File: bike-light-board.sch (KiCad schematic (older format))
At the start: 104 parts, among them J1 KH-TYPE-C-16P, J2 S2B-PH-SM4-TB, P2 WirePad, P3 WirePad, Q1 HX2301A, Q2 L2N7002DW1T1G, Q3 HX2301A, Q4 SMD0805-20, Q5 HX2301A, SW1 SW_Push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

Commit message: update flash chip to 4MB and divider for VBUS
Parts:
- R28: value 47k -> 10k; JCLPCB Part Number C25792 -> C25744; LCSC Part Number C380741 -> (none)
- R29: value 47k -> 5k1; JCLPCB Part Number C25792 -> C25905; LCSC Part Number C380741 -> (none)
- U4: value P25Q40H-SSH-IT -> P25Q32H-SSH-IT; symbol cb_ICs_Memory:P25Q40H-SSH-IT -> cb_ICs_Memory:P25Q32H-SSH-IT; JCLPCB Part Number C194873 -> C194874; Size (none) -> 4MB
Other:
- note removed: "4M external flash"
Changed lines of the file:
@@
 $EndComp
 $Comp
-L cb_ICs_Memory:P25Q40H-SSH-IT U4
+L cb_ICs_Memory:P25Q32H-SSH-IT U4
 U 1 1 610A95B7
 P 7150 8300
 F 0 "U4" H 7630 8296 50  0000 L CNN
-F 1 "P25Q40H-SSH-IT" H 7630 8205 50  0000 L CNN
+F 1 "P25Q32H-SSH-IT" H 7630 8205 50  0000 L CNN
 F 2 "Package_SO:SOIC-8_3.9x4.9mm_P1.27mm" H 7150 7700 50  0001 C CNN
 F 3 "https://www.adestotech.com/wp-content/uploads/DS-AT25SF081_045.pdf" H 7150 8300 50  0001 C CNN
-F 4 "C194873	" H 7150 8300 50  0001 C CNN "JCLPCB Part Number"
+F 4 "4MB" H 7400 8500 50  0000 C CNN "Size"
+F 5 "C194874" H 7150 8300 50  0001 C CNN "JCLPCB Part Number"
 	1    7150 8300
 	1    0    0    -1
@@
 Connection ~ 7150 7450
 NoConn ~ 5300 7950
-Text Notes 7350 8900 0    50   Italic 0
-4M external flash
 $Comp
 L cb_Capacitors-Ceramic:C_0402_50V_COG_20p C17
@@
 P 4300 4550
 F 0 "R28" H 4370 4596 50  0000 L CNN
-F 1 "47k" H 4370 4505 50  0000 L CNN
+F 1 "10k" H 4370 4505 50  0000 L CNN
 F 2 "Resistor_SMD:R_0402_1005Metric" V 4230 4550 50  0001 C CNN
 F 3 "~" H 4300 4550 50  0001 C CNN
-F 4 "C380741" H 4300 4550 50  0001 C CNN "LCSC Part Number"
-F 5 "C25792" H 4300 4550 50  0001 C CNN "JCLPCB Part Number"
+F 4 "C25744" H 4300 4550 50  0001 C CNN "JCLPCB Part Number"
 	1    4300 4550
 	1    0    0    -1
@@
 P 4300 4950
 F 0 "R29" H 4370 4996 50  0000 L CNN
-F 1 "47k" H 4370 4905 50  0000 L CNN
+F 1 "5k1" H 4370 4905 50  0000 L CNN
 F 2 "Resistor_SMD:R_0402_1005Metric" V 4230 4950 50  0001 C CNN
 F 3 "~" H 4300 4950 50  0001 C CNN
-F 4 "C380741" H 4300 4950 50  0001 C CNN "LCSC Part Number"
-F 5 "C25792" H 4300 4950 50  0001 C CNN "JCLPCB Part Number"
+F 4 "C25905" H 4300 4950 50  0001 C CNN "JCLPCB Part Number"
 	1    4300 4950
 	1    0    0    -1

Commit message: update flash chip to faster version
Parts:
- U4: value P25Q32H-SSH-IT -> XT25F32BSOIG; symbol cb_ICs_Memory:P25Q32H-SSH-IT -> cb_ICs_Memory:XT25F32BSOIG
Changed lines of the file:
@@
-	1    0    0    -1
-$EndComp
-$Comp
-L cb_ICs_Memory:P25Q32H-SSH-IT U4
-U 1 1 610A95B7
-P 7150 8300
-F 0 "U4" H 7630 8296 50  0000 L CNN
-F 1 "P25Q32H-SSH-IT" H 7630 8205 50  0000 L CNN
-F 2 "Package_SO:SOIC-8_3.9x4.9mm_P1.27mm" H 7150 7700 50  0001 C CNN
-F 3 "https://www.adestotech.com/wp-content/uploads/DS-AT25SF081_045.pdf" H 7150 8300 50  0001 C CNN
-F 4 "4MB" H 7400 8500 50  0000 C CNN "Size"
-F 5 "C194874" H 7150 8300 50  0001 C CNN "JCLPCB Part Number"
-	1    7150 8300
 	1    0    0    -1
 $EndComp
@@
 Wire Wire Line
 	4850 2900 5100 2900
+$Comp
+L cb_ICs_Memory:XT25F32BSOIG U4
+U 1 1 610A95B7
+P 7150 8300
+F 0 "U4" H 7630 8296 50  0000 L CNN
+F 1 "XT25F32BSOIG" H 7630 8205 50  0000 L CNN
+F 2 "Package_SO:SOIC-8_3.9x4.9mm_P1.27mm" H 7150 7700 50  0001 C CNN
+F 3 "https://datasheet.lcsc.com/lcsc/2005251035_XTX-XT25F32BSOIGU-S_C558851.pdf" H 7150 8300 50  0001 C CNN
+F 4 "4MB" H 7400 8500 50  0000 C CNN "Size"
+F 5 "C194874" H 7150 8300 50  0001 C CNN "JCLPCB Part Number"
+	1    7150 8300
+	1    0    0    -1
+$EndComp
 $EndSCHEMATC

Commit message: add sw pn
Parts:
- SW1: value SW_Push -> TS5220A; symbol Switch:SW_Push -> cb_Switch:TS5220A; JCLPCB Part Number C10852 -> (none); LCSC Part Number C412370 -> (none)
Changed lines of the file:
@@
 $EndComp
 $Comp
-L Switch:SW_Push SW1
+L cb_Switch:TS5220A SW1
 U 1 1 5F08E0CF
 P 13150 6550
 F 0 "SW1" H 13150 6450 50  0000 C CNN
-F 1 "SW_Push" H 13200 6300 50  0001 C CNN
+F 1 "TS5220A" H 13200 6300 50  0001 C CNN
 F 2 "Button_Switch_SMD:SW_SPST_TL3342" H 13150 6750 50  0001 C CNN
-F 3 "~" H 13150 6750 50  0001 C CNN
-F 4 "C412370" H 13150 6550 50  0001 C CNN "LCSC Part Number"
-F 5 "C10852" H 13150 6550 50  0001 C CNN "JCLPCB Part Number"
+F 3 "https://datasheet.lcsc.com/szlcsc/1906201928_SHOU-HAN-TS3625A_C398053.pdf" H 13150 6750 50  0001 C CNN
 	1    13150 6550
 	0    -1   1    0

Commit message: update JCLPCB part numbers
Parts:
- D3, D4, D5, D6, D7, D8: JCLPCB Part Number (none) -> C114586
- Q4: JCLPCB Part Number (none) -> C250858
- SW1: JCLPCB Part Number (none) -> C412370
- SW2, SW3: value STO-060A16AB -> DNP
- U4: JCLPCB Part Number C194874 -> C558851
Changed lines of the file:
@@
 F 3 "" H 12800 4300 50  0001 C CNN
 F 4 "C250858" H 12800 4300 50  0001 C CNN "LCSC Part Number"
+F 5 "C250858" H 12800 4300 50  0001 C CNN "JCLPCB Part Number"
 	1    12800 4300
 	1    0    0    -1
@@
 F 2 "Button_Switch_SMD:SW_SPST_TL3342" H 13150 6750 50  0001 C CNN
 F 3 "https://datasheet.lcsc.com/szlcsc/1906201928_SHOU-HAN-TS3625A_C398053.pdf" H 13150 6750 50  0001 C CNN
+F 4 "C412370" H 13150 6550 50  0001 C CNN "JCLPCB Part Number"
 	1    13150 6550
 	0    -1   1    0
@@
 F 3 "https://cdn-shop.adafruit.com/datasheets/WS2812B.pdf" H 15400 6225 50  0001 L TNN
 F 4 "C114586" H 15300 6600 50  0001 C CNN "LCSC Part Number"
+F 5 "C114586" H 15300 6600 50  0001 C CNN "JCLPCB Part Number"
 	1    15300 6600
 	0    1    1    0
@@
 F 3 "https://cdn-shop.adafruit.com/datasheets/WS2812B.pdf" H 15400 5375 50  0001 L TNN
 F 4 "C114586" H 15300 5750 50  0001 C CNN "LCSC Part Number"
+F 5 "C114586" H 15300 5750 50  0001 C CNN "JCLPCB Part Number"
 	1    15300 5750
 	0    1    1    0
@@
 F 3 "https://cdn-shop.adafruit.com/datasheets/WS2812B.pdf" H 15400 4525 50  0001 L TNN
 F 4 "C114586" H 15300 4900 50  0001 C CNN "LCSC Part Number"
+F 5 "C114586" H 15300 4900 50  0001 C CNN "JCLPCB Part Number"
 	1    15300 4900
 	0    1    1    0
@@
 F 3 "https://cdn-shop.adafruit.com/datasheets/WS2812B.pdf" H 15400 3675 50  0001 L TNN
 F 4 "C114586" H 15300 4050 50  0001 C CNN "LCSC Part Number"
+F 5 "C114586" H 15300 4050 50  0001 C CNN "JCLPCB Part Number"
 	1    15300 4050
 	0    1    1    0
@@
 F 3 "https://cdn-shop.adafruit.com/datasheets/WS2812B.pdf" H 15400 2825 50  0001 L TNN
 F 4 "C114586" H 15300 3200 50  0001 C CNN "LCSC Part Number"
+F 5 "C114586" H 15300 3200 50  0001 C CNN "JCLPCB Part Number"
 	1    15300 3200
 	0    1    1    0
@@
 F 3 "https://cdn-shop.adafruit.com/datasheets/WS2812B.pdf" H 15400 1975 50  0001 L TNN
 F 4 "C114586" H 15300 2350 50  0001 C CNN "LCSC Part Number"
+F 5 "C114586" H 15300 2350 50  0001 C CNN "JCLPCB Part Number"
 	1    15300 2350
 	0    1    1    0
@@
 P 13350 8450
 F 0 "SW2" V 13350 8402 50  0000 R CNN
-F 1 "STO-060A16AB" H 13350 8390 50  0001 C CNN
+F 1 "DNP" H 13350 8390 50  0001 C CNN
 F 2 "footprints:STO-060A16AB" H 13350 8650 50  0001 C CNN
 F 3 "https://media.digikey.com/pdf/Data%20Sheets/Mitsumi%20Elect/STO-060A16AB_R66-7995.pdf" H 13350 8650 50  0001 C CNN
@@
 P 14850 8450
 F 0 "SW3" V 14850 8402 50  0000 R CNN
-F 1 "STO-060A16AB" H 14850 8390 50  0001 C CNN
+F 1 "DNP" H 14850 8390 50  0001 C CNN
 F 2 "footprints:STO-060A16AB" H 14850 8650 50  0001 C CNN
 F 3 "https://media.digikey.com/pdf/Data%20Sheets/Mitsumi%20Elect/STO-060A16AB_R66-7995.pdf" H 14850 8650 50  0001 C CNN
@@
 F 3 "https://datasheet.lcsc.com/lcsc/2005251035_XTX-XT25F32BSOIGU-S_C558851.pdf" H 7150 8300 50  0001 C CNN
 F 4 "4MB" H 7400 8500 50  0000 C CNN "Size"
-F 5 "C194874" H 7150 8300 50  0001 C CNN "JCLPCB Part Number"
+F 5 "C558851" H 7150 8300 50  0001 C CNN "JCLPCB Part Number"
 	1    7150 8300
 	1    0    0    -1

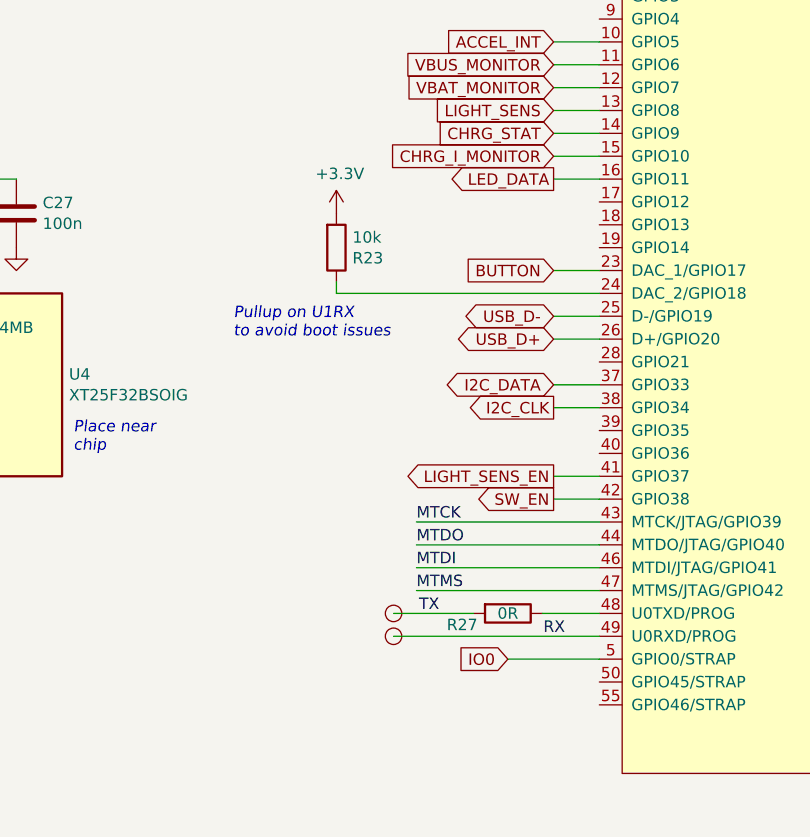
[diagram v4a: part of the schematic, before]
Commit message: add 10k to IO0 pin to fix boot issue
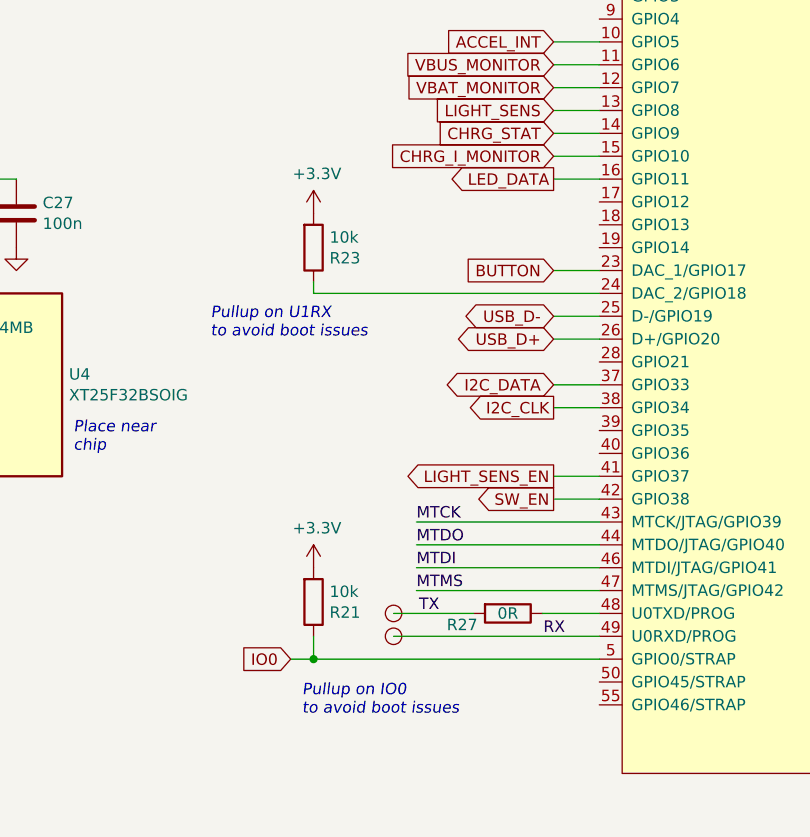
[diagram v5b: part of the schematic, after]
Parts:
- added R21: 10k, Resistor_SMD:R_0402_1005Metric, symbol Device:R
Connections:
- net +3V3: now also R21.2
- net IO0: now also R21.1
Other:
- note added: "Pullup on IO0\nto avoid boot issues"
- moved on the sheet: R23
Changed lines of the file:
@@
 L Device:R R23
 U 1 1 612F8DF5
-P 8800 7750
-F 0 "R23" H 8870 7796 50  0000 L CNN
-F 1 "10k" H 8870 7705 50  0000 L CNN
-F 2 "Resistor_SMD:R_0402_1005Metric" V 8730 7750 50  0001 C CNN
-F 3 "~" H 8800 7750 50  0001 C CNN
-F 4 "C60490" H 8800 7750 50  0001 C CNN "LCSC Part Number"
-F 5 "C25744" H 8800 7750 50  0001 C CNN "JCLPCB Part Number"
-	1    8800 7750
+P 8700 7750
+F 0 "R23" H 8770 7796 50  0000 L CNN
+F 1 "10k" H 8770 7705 50  0000 L CNN
+F 2 "Resistor_SMD:R_0402_1005Metric" V 8630 7750 50  0001 C CNN
+F 3 "~" H 8700 7750 50  0001 C CNN
+F 4 "C60490" H 8700 7750 50  0001 C CNN "LCSC Part Number"
+F 5 "C25744" H 8700 7750 50  0001 C CNN "JCLPCB Part Number"
+	1    8700 7750
 	1    0    0    1
 $EndComp
@@
 L power:+3.3V #PWR0130
 U 1 1 6130F896
-P 8800 7600
-F 0 "#PWR0130" H 8800 7450 50  0001 C CNN
-F 1 "+3.3V" H 8815 7773 50  0000 C CNN
-F 2 "" H 8800 7600 50  0001 C CNN
-F 3 "" H 8800 7600 50  0001 C CNN
-	1    8800 7600
-	1    0    0    -1
-$EndComp
-Wire Wire Line
-	8800 7900 8800 7950
-Text Notes 8350 8150 0    50   Italic 0
+P 8700 7600
+F 0 "#PWR0130" H 8700 7450 50  0001 C CNN
+F 1 "+3.3V" H 8715 7773 50  0000 C CNN
+F 2 "" H 8700 7600 50  0001 C CNN
+F 3 "" H 8700 7600 50  0001 C CNN
+	1    8700 7600
+	1    0    0    -1
+$EndComp
+Wire Wire Line
+	8700 7900 8700 7950
+Text Notes 8250 8150 0    50   Italic 0
 Pullup on U1RX\nto avoid boot issues
 $Comp
@@
 VBUS_IN
 Wire Wire Line
-	8800 7950 9950 7950
-Wire Wire Line
 	2750 2900 3550 2900
 Wire Wire Line
-	9550 9550 9950 9550
+	8600 9550 8700 9550
 Wire Wire Line
 	9050 9350 9400 9350
@@
 Wire Wire Line
 	13200 8250 13100 8250
-Text GLabel 9550 9550 0    50   Input ~ 0
+Text GLabel 8600 9550 0    50   Input ~ 0
 IO0
 Text GLabel 12650 8250 0    50   Output ~ 0
@@
 	1    0    0    -1
 $EndComp
+$Comp
+L Device:R R21
+U 1 1 616AFBAD
+P 8700 9300
+F 0 "R21" H 8770 9346 50  0000 L CNN
+F 1 "10k" H 8770 9255 50  0000 L CNN
+F 2 "Resistor_SMD:R_0402_1005Metric" V 8630 9300 50  0001 C CNN
+F 3 "~" H 8700 9300 50  0001 C CNN
+F 4 "C60490" H 8700 9300 50  0001 C CNN "LCSC Part Number"
+F 5 "C25744" H 8700 9300 50  0001 C CNN "JCLPCB Part Number"
+	1    8700 9300
+	1    0    0    1
+$EndComp
+$Comp
+L power:+3.3V #PWR017
+U 1 1 616AFBB3
+P 8700 9150
+F 0 "#PWR017" H 8700 9000 50  0001 C CNN
+F 1 "+3.3V" H 8715 9323 50  0000 C CNN
+F 2 "" H 8700 9150 50  0001 C CNN
+F 3 "" H 8700 9150 50  0001 C CNN
+	1    8700 9150
+	1    0    0    -1
+$EndComp
+Wire Wire Line
+	8700 7950 9950 7950
+Wire Wire Line
+	8700 9450 8700 9550
+Connection ~ 8700 9550
+Wire Wire Line
+	8700 9550 9950 9550
+Text Notes 8650 9800 0    50   Italic 0
+Pullup on IO0\nto avoid boot issues
 $EndSCHEMATC
